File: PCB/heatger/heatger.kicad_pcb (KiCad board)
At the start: 2 copper layers, 62 x 98 mm, 22 parts, among them J1 RPI, J2 DC command, J3 AC Pilote, J4 USB_B_Micro, U1 TLP3023, U2 TLP3023, U3 TLP3023, U4 TLP3023, U5 P82B715DR

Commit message: add capacitors and gerbers files
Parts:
- added REF**: MountingHole_2.1mm, MountingHole:MountingHole_2.1mm, F.Cu at (152.0, 86.0)
- added REF**: MountingHole_2.1mm, MountingHole:MountingHole_2.1mm, F.Cu at (152.0, 149.0)
- added REF**: MountingHole_2.1mm, MountingHole:MountingHole_2.1mm, F.Cu at (122.0, 86.0)
- added REF**: MountingHole_2.1mm, MountingHole:MountingHole_2.1mm, F.Cu at (122.0, 149.0)
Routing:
- net Net-(J1-Pin_3): track 58.4 -> 57.7 mm
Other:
- outline, holes or cut-outs redrawn

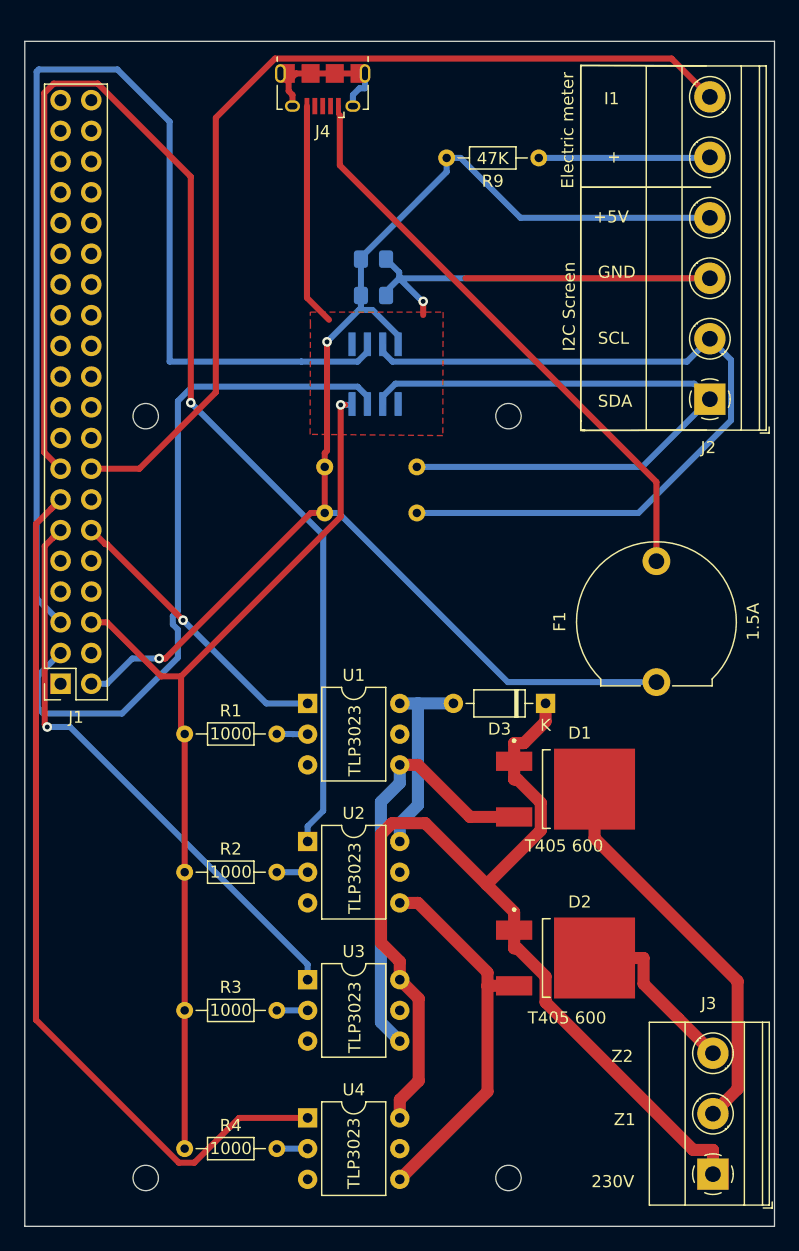
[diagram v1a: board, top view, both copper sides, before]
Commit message: invert wiring for pin headers
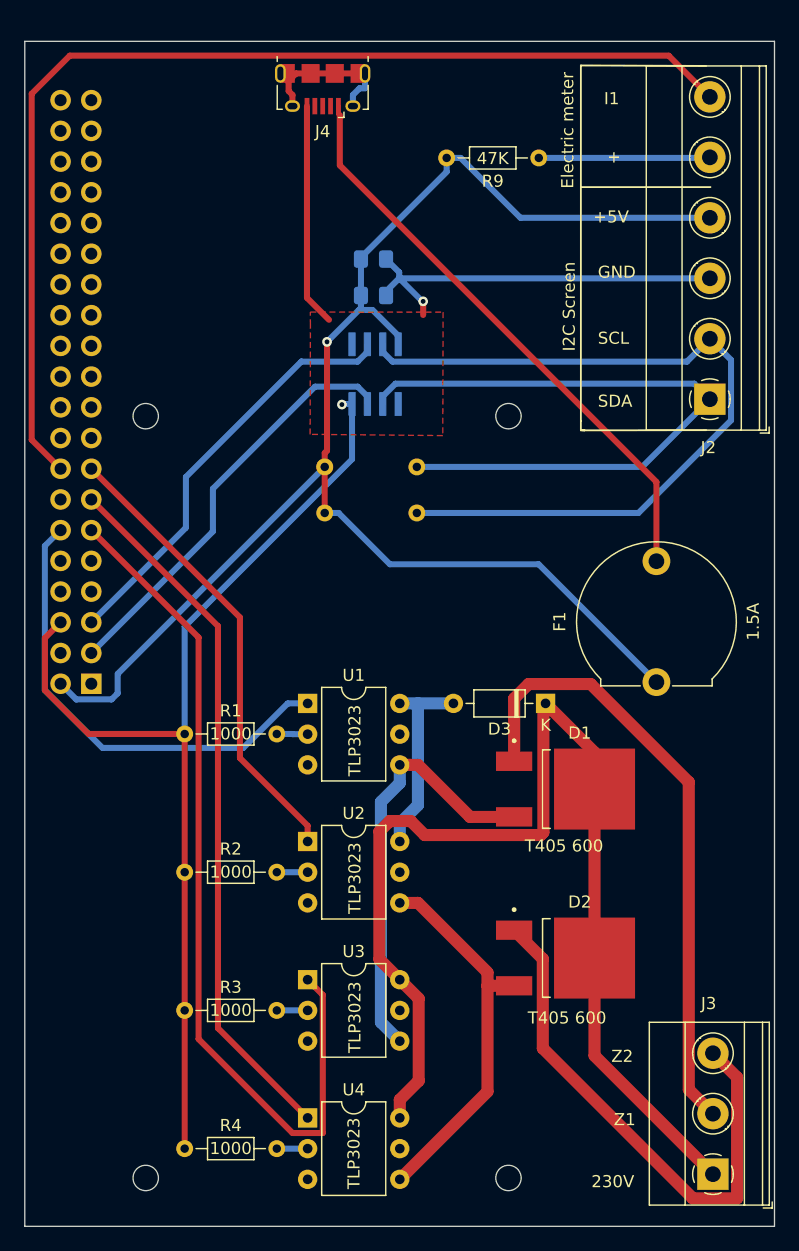
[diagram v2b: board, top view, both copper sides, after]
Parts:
- J1: moved to B.Cu
- R7, R8: value 330 -> 1000
- moved J1 2.54 mm to (117.5, 108.1), turned to 0 degrees
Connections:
- D2 pad 1: Net-(D1-A1) -> Net-(D2-A1)
- D2 pad 2: Net-(D2-A2) -> Net-(D1-A2)
- D3 pad 1: Net-(D1-A1) -> Net-(D1-A2)
- J3 pad 1: Net-(D1-A1) -> Net-(D1-A2)
- J3 pad 2: Net-(D1-A2) -> Net-(D1-A1)
- J3 pad 3: Net-(D2-A2) -> Net-(D2-A1)
- U3 pad 6: Net-(D1-A1) -> Net-(D1-A2)
- U4 pad 6: Net-(D1-A1) -> Net-(D1-A2)
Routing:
- net Net-(J1-Pin_15): track 107.3 -> 38.2 mm, vias 1 -> 0
- net Net-(D1-A2): track 32.6 -> 95.6 mm
- net Net-(J1-Pin_5): track 96.4 -> 35.2 mm
- net Net-(D2-A1): track 0.00 -> 44.8 mm
- net Net-(D1-A1): track 88.9 -> 51.7 mm
- net Net-(J1-Pin_11): track 48.8 -> 72.4 mm, vias 1 -> 0
- net Net-(J1-Pin_3): track 57.7 -> 35.0 mm
- net Net-(D2-A2): track 18.4 -> 0.00 mm
- net Net-(J1-Pin_13): track 73.9 -> 58.6 mm
- net Net-(J1-Pin_12): track 23.8 -> 39.0 mm, vias 1 -> 0
- net Net-(J1-Pin_16): track 79.8 -> 90.8 mm
- net Net-(J1-Pin_6): track 149.9 -> 139.6 mm
- net Net-(J1-Pin_2): track 121.7 -> 127.8 mm, vias 2 -> 1
